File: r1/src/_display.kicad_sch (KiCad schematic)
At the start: 3 parts, among them J4 AFC07-S40ECA-00, Q6 AP2302B

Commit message: Assign footprints
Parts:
- J4: footprint jeffmakes_footprints:D-1206 -> jeffmakes_footprints:AFC07x40-1MP_P0.5mm_Horizontal
- Q6: footprint jeffmakes_footprints:USB-A-short-body-in-cutout-type-strenghening-vias -> Package_TO_SOT_SMD:SOT-23
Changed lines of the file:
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@@
       (effects (font (size 1.27 1.27)) (justify left))
     )
-    (property "Footprint" "jeffmakes_footprints:USB-A-short-body-in-cutout-type-strenghening-vias" (at 132.08 143.51 0)
+    (property "Footprint" "Package_TO_SOT_SMD:SOT-23" (at 132.08 143.51 0)
       (effects (font (size 1.27 1.27)) hide)
     )
@@
       (effects (font (size 1.27 1.27)) (justify left))
     )
-    (property "Footprint" "jeffmakes_footprints:D-1206" (at 158.75 99.06 0)
+    (property "Footprint" "jeffmakes_footprints:AFC07x40-1MP_P0.5mm_Horizontal" (at 158.75 99.06 0)
       (effects (font (size 1.27 1.27)) hide)
     )

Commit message: ERC pass. Schematic complete.
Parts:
- added DISP1: Z280IT008, jeffmakes-footprints:Z280IT009, symbol j_Display:Display_dummy
- J4: footprint jeffmakes_footprints:AFC07x40-1MP_P0.5mm_Horizontal -> jeffmakes-footprints:AFC07x40-1MP_P0.5mm_Horizontal_reverse_pinout
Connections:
- net +3.3V: now also J4.39 (Pin_39)
- net GND: now also J4.38 (Pin_38)
- no-connect marks 1 -> 5
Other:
- note added: "4-wire 8-bit SPI mode (IM=6)"
- note removed: "TODO: Confirm 3/4-wire mode"
- note removed: "TODO: Confirm touch"
- note removed: "TODO: Display symbol and footprint"
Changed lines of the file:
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@@
   (junction (at 147.32 109.22) (diameter 0) (color 0 0 0 0)
   )
+  (junction (at 143.51 147.32) (diameter 0) (color 0 0 0 0)
+  )
   (junction (at 147.32 142.24) (diameter 0) (color 0 0 0 0)
   )
@@
   (junction (at 147.32 106.68) (diameter 0) (color 0 0 0 0)
   )
+  (junction (at 147.32 144.78) (diameter 0) (color 0 0 0 0)
+  )
   (junction (at 151.13 137.16) (diameter 0) (color 0 0 0 0)
   )
@@
   )
   (no_connect (at 153.67 83.82))
+  (no_connect (at 153.67 53.34))
+  (no_connect (at 153.67 50.8))
+  (no_connect (at 153.67 55.88))
+  (no_connect (at 153.67 58.42))
   (wire (pts (xy 147.32 114.3) (xy 153.67 114.3))
     (stroke (width 0) (type default))
@@
     (stroke (width 0) (type default))
   )
+  (wire (pts (xy 143.51 147.32) (xy 143.51 132.08))
+    (stroke (width 0) (type default))
+  )
   (wire (pts (xy 129.54 139.7) (xy 129.54 140.97))
     (stroke (width 0) (type default))
@@
     (stroke (width 0) (type default))
   )
+  (wire (pts (xy 143.51 147.32) (xy 153.67 147.32))
+    (stroke (width 0) (type default))
+  )
   (wire (pts (xy 119.38 146.05) (xy 119.38 148.59))
     (stroke (width 0) (type default))
@@
     (stroke (width 0) (type default))
   )
-  (wire (pts (xy 147.32 142.24) (xy 147.32 156.21))
+  (wire (pts (xy 147.32 142.24) (xy 147.32 144.78))
     (stroke (width 0) (type default))
   )
@@
     (stroke (width 0) (type default))
   )
+  (wire (pts (xy 147.32 144.78) (xy 147.32 156.21))
+    (stroke (width 0) (type default))
+  )
   (wire (pts (xy 153.67 66.04) (xy 143.51 66.04))
     (stroke (width 0) (type default))
@@
     (stroke (width 0) (type default))
   )
+  (wire (pts (xy 147.32 144.78) (xy 153.67 144.78))
+    (stroke (width 0) (type default))
+  )
   (wire (pts (xy 147.32 116.84) (xy 153.67 116.84))
     (stroke (width 0) (type default))
@@
     (stroke (width 0) (type default))
   )
-  (wire (pts (xy 143.51 149.86) (xy 143.51 132.08))
+  (wire (pts (xy 143.51 149.86) (xy 143.51 147.32))
     (stroke (width 0) (type default))
   )
@@
     (effects (font (size 1.27 1.27)) (justify left bottom))
   )
-  (text "TODO: Confirm 3/4-wire mode" (at 68.58 36.83 0)
+  (text "4-wire 8-bit SPI mode (IM=6)\n" (at 87.63 78.105 0)
     (effects (font (size 1.27 1.27)) (justify left bottom))
   )
@@
     (effects (font (size 1.27 1.27)) (justify left bottom))
   )
-  (text "TODO: Display symbol and footprint" (at 68.58 41.91 0)
-    (effects (font (size 1.27 1.27)) (justify left bottom))
-  )
   (text "RD" (at 161.2511 78.6778 0)
     (effects (font (size 1.27 1.27)) (justify left bottom))
@@
   )
   (text "DB9" (at 161.29 114.3 0)
-    (effects (font (size 1.27 1.27)) (justify left bottom))
-  )
-  (text "TODO: Confirm touch" (at 68.58 39.37 0)
     (effects (font (size 1.27 1.27)) (justify left bottom))
   )
@@
       (effects (font (size 1.27 1.27)) (justify left))
     )
-    (property "Footprint" "jeffmakes_footprints:AFC07x40-1MP_P0.5mm_Horizontal" (at 158.75 99.06 0)
+    (property "Footprint" "jeffmakes-footprints:AFC07x40-1MP_P0.5mm_Horizontal_reverse_pinout" (at 158.75 99.06 0)
       (effects (font (size 1.27 1.27)) hide)
     )
@@
         )
       )
+    )
+  )
+  (symbol (lib_id "j_Display:Display_dummy") (at 205.74 98.425 0) (unit 1)
+    (in_bom yes) (on_board yes) (dnp no) (fields_autoplaced)
+    (property "Reference" "DISP1" (at 215.9 97.79 0)
+      (effects (font (size 1.27 1.27)) (justify left))
+    )
+    (property "Value" "Z280IT008" (at 215.9 100.33 0)
+      (effects (font (size 1.27 1.27)) (justify left))
+    )
+    (property "Footprint" "jeffmakes-footprints:Z280IT009" (at 205.74 98.425 0)
+      (effects (font (size 1.27 1.27)) hide)
+    )
+    (property "Datasheet" "" (at 205.74 98.425 0)
+      (effects (font (size 1.27 1.27)) hide)
+    )
+    (instances
+      (project "tr23-outline-test-r1"
+        (path "/a8e3e111-1bac-465b-987f-3974eb7eae63"
+          (reference "DISP1") (unit 1)
+        )
+      )
+      (project "tr23-badge-r1"
+        (path "/ab725fe7-4504-40ef-b6af-82d065d00fb6"
+          (reference "DISP1") (unit 1)
+        )
+        (path "/ab725fe7-4504-40ef-b6af-82d065d00fb6/00000000-0000-0000-0000-00005e536877"
+          (reference "DISP1") (unit 1)
+        )
+      )

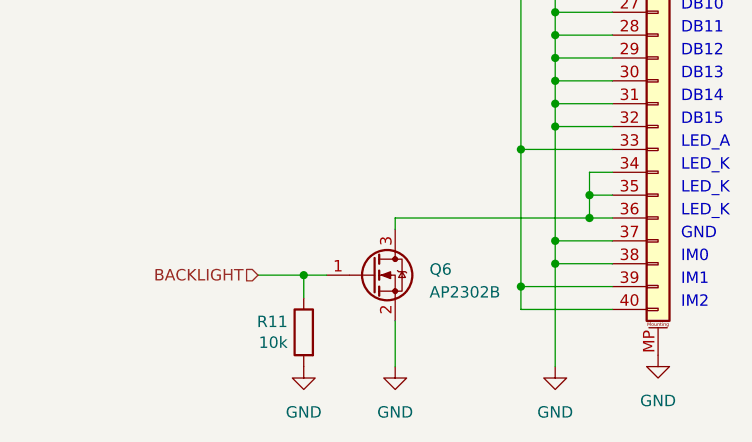
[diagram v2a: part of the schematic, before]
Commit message: Current limiting resistor for backlight
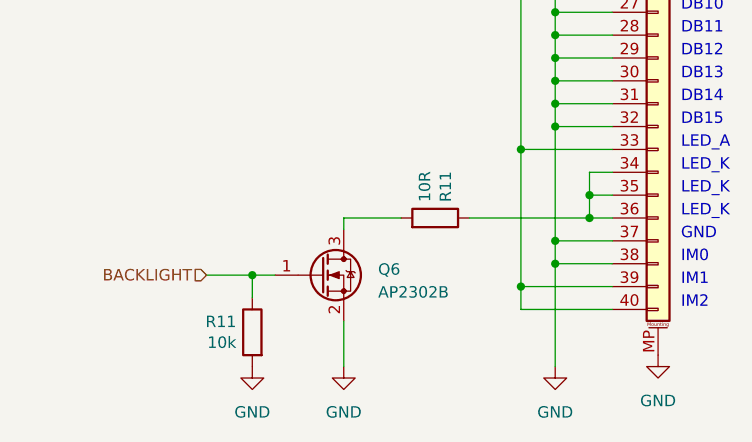
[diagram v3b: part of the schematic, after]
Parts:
- added R11: 10R, Resistor_SMD:R_0402_1005Metric, symbol Device:R
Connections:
- net at J4.34 (Pin_34), J4.35 (Pin_35), J4.36 (Pin_36): now also R11.1; no longer Q6.3 (D)
- new net: Q6.3 (D), R11.2
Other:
- moved on the sheet: Q6, R11
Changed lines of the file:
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@@
 (kicad_sch (version 20230221) (generator eeschema)
   (paper "A4")
-  (junction (at 119.38 146.05) (diameter 0) (color 0 0 0 0)
+  (junction (at 113.665 146.05) (diameter 0) (color 0 0 0 0)
   )
   (junction (at 147.32 124.46) (diameter 0) (color 0 0 0 0)
@@
     (stroke (width 0) (type default))
   )
-  (wire (pts (xy 129.54 151.13) (xy 129.54 156.21))
+  (wire (pts (xy 123.825 151.13) (xy 123.825 156.21))
     (stroke (width 0) (type default))
   )
@@
     (stroke (width 0) (type default))
   )
-  (wire (pts (xy 151.13 139.7) (xy 129.54 139.7))
+  (wire (pts (xy 151.13 139.7) (xy 137.795 139.7))
     (stroke (width 0) (type default))
   )
@@
     (stroke (width 0) (type default))
   )
-  (wire (pts (xy 119.38 146.05) (xy 121.92 146.05))
+  (wire (pts (xy 113.665 146.05) (xy 116.205 146.05))
     (stroke (width 0) (type default))
   )
@@
     (stroke (width 0) (type default))
   )
-  (wire (pts (xy 129.54 139.7) (xy 129.54 140.97))
+  (wire (pts (xy 123.825 139.7) (xy 123.825 140.97))
     (stroke (width 0) (type default))
   )
@@
     (stroke (width 0) (type default))
   )
-  (wire (pts (xy 119.38 146.05) (xy 119.38 148.59))
+  (wire (pts (xy 113.665 146.05) (xy 113.665 148.59))
     (stroke (width 0) (type default))
   )
@@
     (stroke (width 0) (type default))
   )
-  (wire (pts (xy 114.3 146.05) (xy 119.38 146.05))
+  (wire (pts (xy 108.585 146.05) (xy 113.665 146.05))
     (stroke (width 0) (type default))
   )
@@
     (stroke (width 0) (type default))
   )
+  (wire (pts (xy 130.175 139.7) (xy 123.825 139.7))
+    (stroke (width 0) (type default))
+  )
   (wire (pts (xy 147.32 121.92) (xy 153.67 121.92))
     (stroke (width 0) (type default))
@@
     (effects (font (size 1.27 1.27)) (justify left bottom))
   )
-  (hierarchical_label "BACKLIGHT" (shape input) (at 114.3 146.05 180) (fields_autoplaced)
+  (hierarchical_label "BACKLIGHT" (shape input) (at 108.585 146.05 180) (fields_autoplaced)
     (effects (font (size 1.27 1.27)) (justify right))
   )
@@
     )
   )
-  (symbol (lib_id "Device:R") (at 119.38 152.4 0) (mirror y) (unit 1)
+  (symbol (lib_id "Device:R") (at 113.665 152.4 0) (mirror y) (unit 1)
     (in_bom yes) (on_board yes) (dnp no)
-    (property "Reference" "R11" (at 117.602 151.2316 0)
-      (effects (font (size 1.27 1.27)) (justify left))
-    )
-    (property "Value" "10k" (at 117.602 153.543 0)
-      (effects (font (size 1.27 1.27)) (justify left))
-    )
-    (property "Footprint" "Resistor_SMD:R_0402_1005Metric" (at 121.158 152.4 90)
-      (effects (font (size 1.27 1.27)) hide)
-    )
-    (property "Datasheet" "~" (at 119.38 152.4 0)
+    (property "Reference" "R11" (at 111.887 151.2316 0)
+      (effects (font (size 1.27 1.27)) (justify left))
+    )
+    (property "Value" "10k" (at 111.887 153.543 0)
+      (effects (font (size 1.27 1.27)) (justify left))
+    )
+    (property "Footprint" "Resistor_SMD:R_0402_1005Metric" (at 115.443 152.4 90)
+      (effects (font (size 1.27 1.27)) hide)
+    )
+    (property "Datasheet" "~" (at 113.665 152.4 0)
       (effects (font (size 1.27 1.27)) hide)
     )
@@
     )
   )
-  (symbol (lib_id "Device:Q_NMOS_GSD") (at 127 146.05 0) (unit 1)
+  (symbol (lib_id "Device:Q_NMOS_GSD") (at 121.285 146.05 0) (unit 1)
     (in_bom yes) (on_board yes) (dnp no) (fields_autoplaced)
-    (property "Reference" "Q6" (at 133.35 145.415 0)
-      (effects (font (size 1.27 1.27)) (justify left))
-    )
-    (property "Value" "AP2302B" (at 133.35 147.955 0)
-      (effects (font (size 1.27 1.27)) (justify left))
-    )
-    (property "Footprint" "Package_TO_SOT_SMD:SOT-23" (at 132.08 143.51 0)
-      (effects (font (size 1.27 1.27)) hide)
-    )
-    (property "Datasheet" "~" (at 127 146.05 0)
-      (effects (font (size 1.27 1.27)) hide)
-    )
-    (property "MPN" "AP2302B" (at 127 146.05 0)
-      (effects (font (size 1.27 1.27)) hide)
-    )
-    (property "LCSC" "C5224180" (at 127 146.05 0)
+    (property "Reference" "Q6" (at 127.635 145.415 0)
+      (effects (font (size 1.27 1.27)) (justify left))
+    )
+    (property "Value" "AP2302B" (at 127.635 147.955 0)
+      (effects (font (size 1.27 1.27)) (justify left))
+    )
+    (property "Footprint" "Package_TO_SOT_SMD:SOT-23" (at 126.365 143.51 0)
+      (effects (font (size 1.27 1.27)) hide)
+    )
+    (property "Datasheet" "~" (at 121.285 146.05 0)
+      (effects (font (size 1.27 1.27)) hide)
+    )
+    (property "MPN" "AP2302B" (at 121.285 146.05 0)
+      (effects (font (size 1.27 1.27)) hide)
+    )
+    (property "LCSC" "C5224180" (at 121.285 146.05 0)
       (effects (font (size 1.27 1.27)) hide)
     )
@@
     )
   )
-  (symbol (lib_id "power:GND") (at 119.38 156.21 0) (unit 1)
+  (symbol (lib_id "power:GND") (at 113.665 156.21 0) (unit 1)
     (in_bom yes) (on_board yes) (dnp no) (fields_autoplaced)
-    (property "Reference" "#PWR040" (at 119.38 162.56 0)
-      (effects (font (size 1.27 1.27)) hide)
-    )
-    (property "Value" "GND" (at 119.38 161.29 0)
+    (property "Reference" "#PWR040" (at 113.665 162.56 0)
+      (effects (font (size 1.27 1.27)) hide)
+    )
+    (property "Value" "GND" (at 113.665 161.29 0)
       (effects (font (size 1.27 1.27)))
     )
-    (property "Footprint" "" (at 119.38 156.21 0)
-      (effects (font (size 1.27 1.27)) hide)
-    )
-    (property "Datasheet" "" (at 119.38 156.21 0)
+    (property "Footprint" "" (at 113.665 156.21 0)
+      (effects (font (size 1.27 1.27)) hide)
+    )
+    (property "Datasheet" "" (at 113.665 156.21 0)
       (effects (font (size 1.27 1.27)) hide)
     )
@@
     )
   )
-  (symbol (lib_id "power:GND") (at 129.54 156.21 0) (unit 1)
+  (symbol (lib_id "power:GND") (at 123.825 156.21 0) (unit 1)
     (in_bom yes) (on_board yes) (dnp no) (fields_autoplaced)
-    (property "Reference" "#PWR041" (at 129.54 162.56 0)
-      (effects (font (size 1.27 1.27)) hide)
-    )
-    (property "Value" "GND" (at 129.54 161.29 0)
+    (property "Reference" "#PWR041" (at 123.825 162.56 0)
+      (effects (font (size 1.27 1.27)) hide)
+    )
+    (property "Value" "GND" (at 123.825 161.29 0)
       (effects (font (size 1.27 1.27)))
     )
-    (property "Footprint" "" (at 129.54 156.21 0)
-      (effects (font (size 1.27 1.27)) hide)
-    )
-    (property "Datasheet" "" (at 129.54 156.21 0)
+    (property "Footprint" "" (at 123.825 156.21 0)
+      (effects (font (size 1.27 1.27)) hide)
+    )
+    (property "Datasheet" "" (at 123.825 156.21 0)
       (effects (font (size 1.27 1.27)) hide)
     )
@@
         )
       )
+    )
+  )
+  (symbol (lib_id "Device:R") (at 133.985 139.7 270) (mirror x) (unit 1)
+    (in_bom yes) (on_board yes) (dnp no)
+    (property "Reference" "R11" (at 135.1534 137.922 0)
+      (effects (font (size 1.27 1.27)) (justify left))
+    )
+    (property "Value" "10R" (at 132.842 137.922 0)
+      (effects (font (size 1.27 1.27)) (justify left))
+    )
+    (property "Footprint" "Resistor_SMD:R_0402_1005Metric" (at 133.985 141.478 90)
+      (effects (font (size 1.27 1.27)) hide)
+    )
+    (property "Datasheet" "~" (at 133.985 139.7 0)
+      (effects (font (size 1.27 1.27)) hide)
+    )
+    (pin "1")
+    (pin "2")
+    (instances
+      (project "tr23-badge-r1"
+        (path "/ab725fe7-4504-40ef-b6af-82d065d00fb6/00000000-0000-0000-0000-00005ddaba4a"
+          (reference "R11") (unit 1)
+        )
+        (path "/ab725fe7-4504-40ef-b6af-82d065d00fb6/00000000-0000-0000-0000-00005e536877"
+          (reference "R32") (unit 1)
+        )
+      )

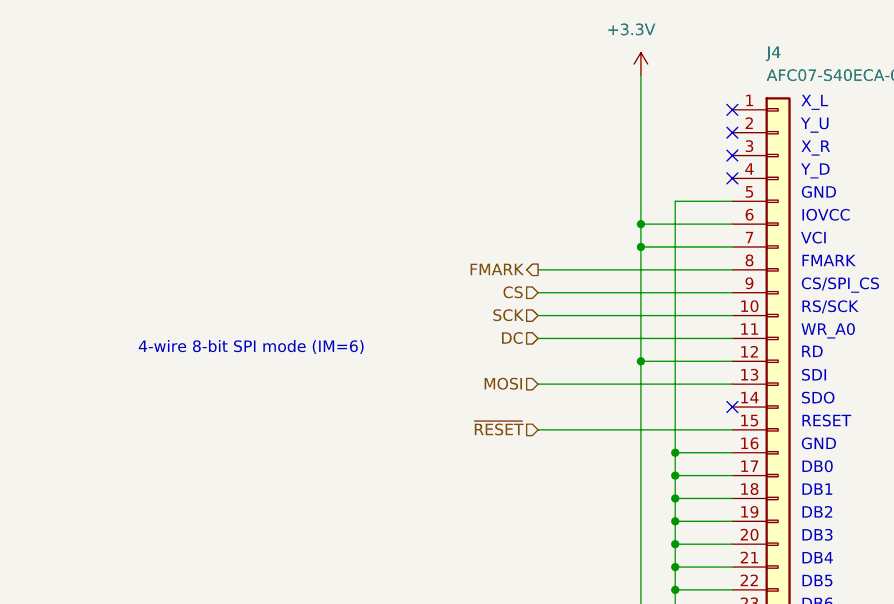
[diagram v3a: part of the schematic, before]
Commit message: Add some test pads to the display bus
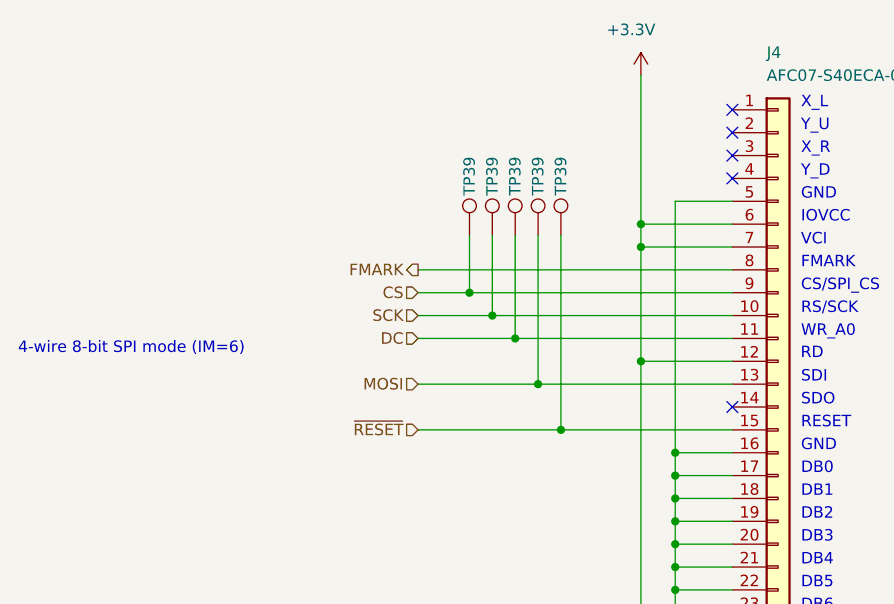
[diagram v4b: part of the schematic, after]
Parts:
- added TP39 (x5): ~, TestPoint:TestPoint_Pad_D1.0mm, symbol Connector:TestPoint
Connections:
- net CS: now also TP39.1
- net DC: now also TP39.1
- net MOSI: now also TP39.1
- net SCK: now also TP39.1
- net ~{RESET}: now also TP39.1

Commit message: Exclude test pads, graphics, etc., from BOM
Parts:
- DISP1, TP39: now left out of the parts list
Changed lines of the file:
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@@
   )
   (symbol (lib_id "Connector:TestPoint") (at 132.08 64.77 0) (unit 1)
-    (in_bom yes) (on_board yes) (dnp no)
+    (in_bom no) (on_board yes) (dnp no)
     (property "Reference" "TP39" (at 132.08 60.325 90)
       (effects (font (size 1.27 1.27)) (justify left))
@@
   )
   (symbol (lib_id "Connector:TestPoint") (at 124.46 64.77 0) (unit 1)
-    (in_bom yes) (on_board yes) (dnp no)
+    (in_bom no) (on_board yes) (dnp no)
     (property "Reference" "TP39" (at 124.46 60.325 90)
       (effects (font (size 1.27 1.27)) (justify left))
@@
   )
   (symbol (lib_id "Connector:TestPoint") (at 127 64.77 0) (unit 1)
-    (in_bom yes) (on_board yes) (dnp no)
+    (in_bom no) (on_board yes) (dnp no)
     (property "Reference" "TP39" (at 127 60.325 90)
       (effects (font (size 1.27 1.27)) (justify left))
@@
   )
   (symbol (lib_id "Connector:TestPoint") (at 134.62 64.77 0) (unit 1)
-    (in_bom yes) (on_board yes) (dnp no)
+    (in_bom no) (on_board yes) (dnp no)
     (property "Reference" "TP39" (at 134.62 60.325 90)
       (effects (font (size 1.27 1.27)) (justify left))
@@
   )
   (symbol (lib_id "j_Display:Display_dummy") (at 205.74 98.425 0) (unit 1)
-    (in_bom yes) (on_board yes) (dnp no) (fields_autoplaced)
+    (in_bom no) (on_board yes) (dnp no) (fields_autoplaced)
     (property "Reference" "DISP1" (at 215.9 97.79 0)
       (effects (font (size 1.27 1.27)) (justify left))
@@
   )
   (symbol (lib_id "Connector:TestPoint") (at 129.54 64.77 0) (unit 1)
-    (in_bom yes) (on_board yes) (dnp no)
+    (in_bom no) (on_board yes) (dnp no)
     (property "Reference" "TP39" (at 129.54 60.325 90)
       (effects (font (size 1.27 1.27)) (justify left))
